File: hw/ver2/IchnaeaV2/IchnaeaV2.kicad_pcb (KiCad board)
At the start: 4 copper layers, 100 x 100 mm, 398 parts, among them J1 Screw_Terminal_01x09, J2 Screw_Terminal_01x09, J3 Screw_Terminal_01x09, J5 FanConnector, J6 Debug, J7 BMS_Serial, P1 USB_C_Plug_USB2.0, Q1 BSS138, Q10 MCAC80N10Y, Q11 MCAC80N10Y, Q12 MCAC80N10Y, Q13 MCAC80N10Y, Q14 MCAC80N10Y, Q15 MCAC80N10Y, Q16 MCAC80N10Y, Q17 MCAC80N10Y, Q18 MCAC80N10Y, Q19 MCAC80N10Y, Q2 MCAC80N10Y, Q20 MCAC80N10Y, Q21 MCAC80N10Y, Q22 MCAC80N10Y, Q23 MCAC80N10Y, Q24 MCAC80N10Y, Q25 MCAC80N10Y, Q26 BSS138, Q27 BSS84, Q28 BSS138, Q29 BSS138, Q3 MCAC80N10Y, Q30 BSS138, Q4 MCAC80N10Y, Q5 MCAC80N10Y, Q6 MCAC80N10Y, Q7 MCAC80N10Y, Q8 MCAC80N10Y, Q9 MCAC80N10Y, SW1 Boot, SW2 Reset, U1 LTC7871, U10 W25Q32JVZP, U11 RP2040, U12 LM1117MP-5.0, U13 LM1117MP-3.3, U14 W25Q32JVZP, U2 HIP2210, U3 HIP2210, U4 HIP2210, U5 HIP2210, U6 HIP2210, U7 HIP2210, U8 AP66200FVBW-13, U9 74HC4051PW, Y1 12MHz

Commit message: Sync work
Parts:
- added D2: ESD9B5.0ST5G, Diode_SMD:D_SOD-923, F.Cu at (87.8, 105.1)
- added D21: ESD9B5.0ST5G, Diode_SMD:D_SOD-923, F.Cu at (87.8, 109.0)
- added D22: SMAJ90A, Diode_SMD:D_SMA, F.Cu at (123.2, 58.8)
- added D23: SMAJ60A, Diode_SMD:D_SMA, F.Cu at (166.8, 58.8)
- added D24: ESD9B5.0ST5G, Diode_SMD:D_SOD-923, F.Cu at (78.1, 140.5)
- added D3: ESD9B5.0ST5G, Diode_SMD:D_SOD-923, F.Cu at (87.8, 107.1)
- added GD1: 90V-2kA, Fuse:Fuse_1812_4532Metric_Pad1.30x3.40mm_HandSolder, F.Cu at (119.3, 58.8)
- added GD2: 90V-2kA, Fuse:Fuse_1812_4532Metric_Pad1.30x3.40mm_HandSolder, F.Cu at (170.5, 58.8)
- added Q31: BSS138, Package_TO_SOT_SMD:SOT-23, F.Cu at (84.0, 106.5)
- added Q32: BSS138, Package_TO_SOT_SMD:SOT-23, F.Cu at (84.0, 111.2)
- added Q33: BSS138, Package_TO_SOT_SMD:SOT-23, F.Cu at (84.0, 115.8)
- added Q34: BSS138, Package_TO_SOT_SMD:SOT-23, F.Cu at (84.0, 120.4)
- added R124: 100, Resistor_SMD:R_0603_1608Metric, F.Cu at (92.1, 110.7)
- added R125: 10k, Resistor_SMD:R_0603_1608Metric, F.Cu at (92.1, 113.2)
- added R126: 100, Resistor_SMD:R_0603_1608Metric, F.Cu at (92.1, 115.7)
- added R127: 10k, Resistor_SMD:R_0603_1608Metric, F.Cu at (92.1, 118.2)
- added R128: 100, Resistor_SMD:R_0603_1608Metric, F.Cu at (92.1, 120.7)
- added R129: 10k, Resistor_SMD:R_0603_1608Metric, F.Cu at (92.1, 123.3)
- added R53: 100k, Resistor_SMD:R_1206_3216Metric, F.Cu at (126.2, 58.8)
- added R55: 100k, Resistor_SMD:R_1206_3216Metric, F.Cu at (163.9, 58.8)
- added TP72: TestPoint, TestPoint:TestPoint_Pad_D1.0mm, F.Cu at (120.0, 148.8)
- added TP73: TestPoint, TestPoint:TestPoint_Pad_D1.0mm, F.Cu at (113.5, 150.5)
- added TP74: TestPoint, TestPoint:TestPoint_Pad_D1.0mm, F.Cu at (115.2, 150.5)
- R106: value 6.2k-0.25w -> 10k; footprint Resistor_SMD:R_1206_3216Metric_Pad1.30x1.75mm_HandSolder -> Resistor_SMD:R_0603_1608Metric
- R31, R35, R78, R81, R93: footprint Resistor_SMD:R_0603_1608Metric -> Resistor_SMD:R_0805_2012Metric
- R33, R39: footprint Resistor_SMD:R_0603_1608Metric_Pad0.98x0.95mm_HandSolder -> Resistor_SMD:R_0805_2012Metric
- R94: value 6.2k-0.25w -> 100; footprint Resistor_SMD:R_1206_3216Metric_Pad1.30x1.75mm_HandSolder -> Resistor_SMD:R_0603_1608Metric
- moved R97 152.1 mm to (182.6, 151.7)
- moved R96 145.4 mm to (174.3, 149.6)
- moved D14 136.7 mm to (185.4, 149.4)
- moved D15 136.7 mm to (185.4, 151.4)
- moved R123 130.5 mm to (182.4, 149.4), turned to 180 degrees
- moved R85 113.1 mm to (143.6, 128.9)
- moved R84 111.3 mm to (123.7, 152.8), turned to 90 degrees
- moved C23 111.0 mm to (105.1, 152.5), turned to -90 degrees
- moved R94 103.1 mm to (92.1, 105.7), turned to 0 degrees
- moved R106 100.7 mm to (92.1, 108.2), turned to 0 degrees
- moved R89 88.8 mm to (103.6, 152.5), turned to -90 degrees
- moved D16 67.1 mm to (115.2, 152.5), turned to 90 degrees
- moved D17 65.1 mm to (113.5, 152.5), turned to 90 degrees
- moved C87 52.1 mm to (128.7, 139.0), turned to 90 degrees
- moved C84 48.6 mm to (123.2, 128.6), turned to 90 degrees
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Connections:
- net /ControlStage/RUN renamed RUN
- net /ControlStage/SWCLK renamed SWCLK
- net /ControlStage/SWDATA renamed SWDATA
- net /ControlStage/UART0_RX renamed UART0_RX
- net /ControlStage/UART0_TX renamed UART0_TX
- net /ControlStage/UART1_RX renamed UART1_RX
- net /ControlStage/UART1_TX renamed UART1_TX
- D14 pad 2: /ControlStage/FAN_CTL -> FAN_CTL
- D15 pad 2: /ControlStage/FAN_SENSE -> FAN_SENSE
- D19 pad 1: /ControlStage/USB_D- -> Net-(D19-A1)
- D20 pad 1: /ControlStage/USB_D+ -> Net-(D20-A1)
- D5 pad 1: /ControlStage/LED_STATUS_0 -> Net-(D5-K)
- D6 pad 1: /ControlStage/LED_STATUS_1 -> Net-(D6-K)
- D7 pad 1: /ControlStage/LED_STATUS_2 -> Net-(D7-K)
- D8 pad 1: /ControlStage/LED_STATUS_3 -> Net-(D8-K)
- P1 pad A6: /ControlStage/USB_D+ -> Net-(D20-A1)
- P1 pad A7: /ControlStage/USB_D- -> Net-(D19-A1)
- P1 pad B6: /ControlStage/USB_D+ -> Net-(D20-A1)
- P1 pad B7: /ControlStage/USB_D- -> Net-(D19-A1)
- R106 pad 2: VHIGH -> Net-(Q34-G)
- R123 pad 1: /ControlStage/FAN_SENSE -> FAN_SENSE
- R94 pad 1: GND -> Net-(Q34-G)
- R94 pad 2: VLOW -> LED_STATUS_3
- R96 pad 1: /ControlStage/FAN_SENSE -> FAN_SENSE
- R97 pad 2: /ControlStage/FAN_CTL -> FAN_CTL
- R98 pad 1: Net-(U11-USB_DP) -> USB_D-
- R98 pad 2: /ControlStage/USB_D+ -> Net-(D19-A1)
- R99 pad 1: Net-(U11-USB_DM) -> USB_D+
- R99 pad 2: /ControlStage/USB_D- -> Net-(D20-A1)
- U11 pad 11: unconnected-(U11-GPIO8-Pad11) -> LTC_CCM
- U11 pad 12: unconnected-(U11-GPIO9-Pad12) -> LTC_DCM
- U11 pad 13: unconnected-(U11-GPIO10-Pad13) -> LTC_SYNC
- U11 pad 14: unconnected-(U11-GPIO11-Pad14) -> /ControlStage/CTL_LTC_PWM_EN
- U11 pad 29: unconnected-(U11-GPIO18-Pad29) -> LED_STATUS_0
- U11 pad 30: unconnected-(U11-GPIO19-Pad30) -> LED_STATUS_1
- U11 pad 34: /ControlStage/FAN_CTL -> LED_STATUS_2
- U11 pad 35: /ControlStage/FAN_SENSE -> LED_STATUS_3
- U11 pad 36: unconnected-(U11-GPIO24-Pad36) -> FAN_CTL
- U11 pad 37: unconnected-(U11-GPIO25-Pad37) -> FAN_SENSE
- U11 pad 46: Net-(U11-USB_DM) -> USB_D-
- U11 pad 47: Net-(U11-USB_DP) -> USB_D+
- U11 pad 6: unconnected-(U11-GPIO4-Pad6) -> ADC_SEL_2
- U11 pad 7: unconnected-(U11-GPIO5-Pad7) -> ADC_SEL_1
- U11 pad 8: unconnected-(U11-GPIO6-Pad8) -> ADC_SEL_0
- U11 pad 9: unconnected-(U11-GPIO7-Pad9) -> LTC_RUN
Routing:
- net GND: track 183.5 -> 265.7 mm, vias 204 -> 223
- net (no net): track 0.00 -> 64.8 mm
- net VHIGH: track 0.00 -> 42.2 mm
- net +3.3V: track 0.00 -> 22.9 mm, vias 0 -> 12
- net /ControlStage/QSPI_SS: track 0.00 -> 22.2 mm, vias 0 -> 2
- net +5V: track 0.00 -> 18.6 mm, vias 0 -> 9
- net Net-(U10-DO(IO1)): track 0.00 -> 15.9 mm
- net Net-(U10-IO2): track 0.00 -> 14.0 mm
- net RUN: track 0.00 -> 12.6 mm
- net Net-(D4-A): track 0.00 -> 12.1 mm
- net Net-(D16-A2): track 0.00 -> 12.1 mm
- net Net-(U12-VI): track 0.00 -> 11.8 mm
- net Net-(P1-CC2): track 0.00 -> 10.9 mm, vias 0 -> 1
- net Net-(P1-CC1): track 0.00 -> 10.1 mm, vias 0 -> 1
- net +1V1: track 0.00 -> 8.57 mm, vias 0 -> 5
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- added copper zone on F.Cu, net +1V1
- added copper zone on F.Cu, net +3.3V
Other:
- board text added: "0"
- board text added: "1"
- board text added: "2"
- board text added: "3"
- board text added: "BOOT"
- board text added: "RESET"

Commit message: Sync to main pc
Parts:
- removed C92: 100nF, Capacitor_SMD:C_0603_1608Metric
- added TP75: TestPoint, TestPoint:TestPoint_Pad_D1.0mm, F.Cu at (132.4, 125.1)
- added TP76: TestPoint, TestPoint:TestPoint_Pad_D1.0mm, F.Cu at (132.4, 120.0)
- moved C104 85.2 mm to (148.9, 132.9)
- moved TP67 77.2 mm to (153.8, 133.6)
- moved TP68 77.2 mm to (153.8, 136.6)
- moved TP69 77.2 mm to (153.8, 139.7)
- moved TP70 77.2 mm to (153.8, 142.7)
- moved R120 73.2 mm to (148.9, 131.3)
- moved C100 65.9 mm to (155.7, 147.1)
- moved C102 65.9 mm to (155.7, 152.1)
- moved R108 65.9 mm to (159.8, 147.1)
- moved R109 65.9 mm to (159.8, 149.6)
- moved R110 65.9 mm to (159.8, 152.1)
- moved R116 65.9 mm to (157.8, 144.5)
- moved C88 55.4 mm to (123.2, 127.4), turned to 90 degrees
- moved C89 49.4 mm to (118.1, 133.2), turned to 180 degrees
- moved C91 49.2 mm to (129.5, 133.2)
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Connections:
- JP3 pad 3: /ControlStage/SPI1_TX -> /ControlStage/SPI0_TX
- JP4 pad 1: /ControlStage/SPI1_TX -> /ControlStage/SPI0_TX
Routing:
- net GND: track 265.7 -> 298.0 mm, vias 223 -> 233
- net SWDATA: track 0.00 -> 31.3 mm
- net RUN: track 12.6 -> 43.7 mm
- net SWCLK: track 0.00 -> 29.7 mm
- net Net-(U11-XIN): track 0.00 -> 20.0 mm
- net Net-(U11-XOUT): track 0.00 -> 18.8 mm
- net UART0_TX: track 0.00 -> 18.5 mm
- net UART1_TX: track 0.00 -> 17.1 mm
- net UART0_RX: track 0.00 -> 16.1 mm
- net UART1_RX: track 0.00 -> 15.8 mm
- net +1V1: track 8.57 -> 18.0 mm, vias 5 -> 6
- net Net-(J7-Pin_2): track 0.00 -> 9.14 mm
- net Net-(J6-Pin_2): track 0.00 -> 8.72 mm
- net +3.3V: track 22.9 -> 28.3 mm, vias 12 -> 13
- net Net-(J7-Pin_1): track 0.00 -> 4.10 mm
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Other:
- board text added: "G"
- board text added: "R"
- board text added: "T"

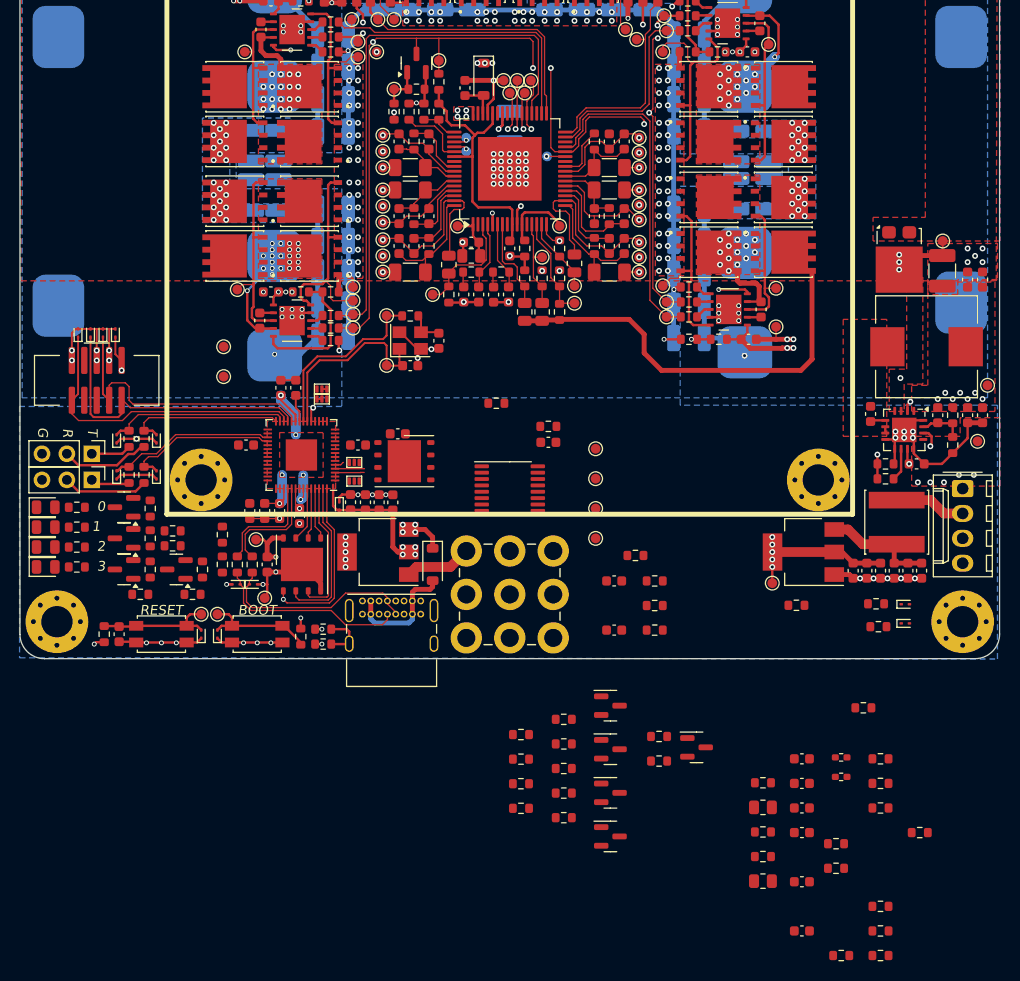
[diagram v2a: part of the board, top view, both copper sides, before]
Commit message: Finish the initial rough route/placement
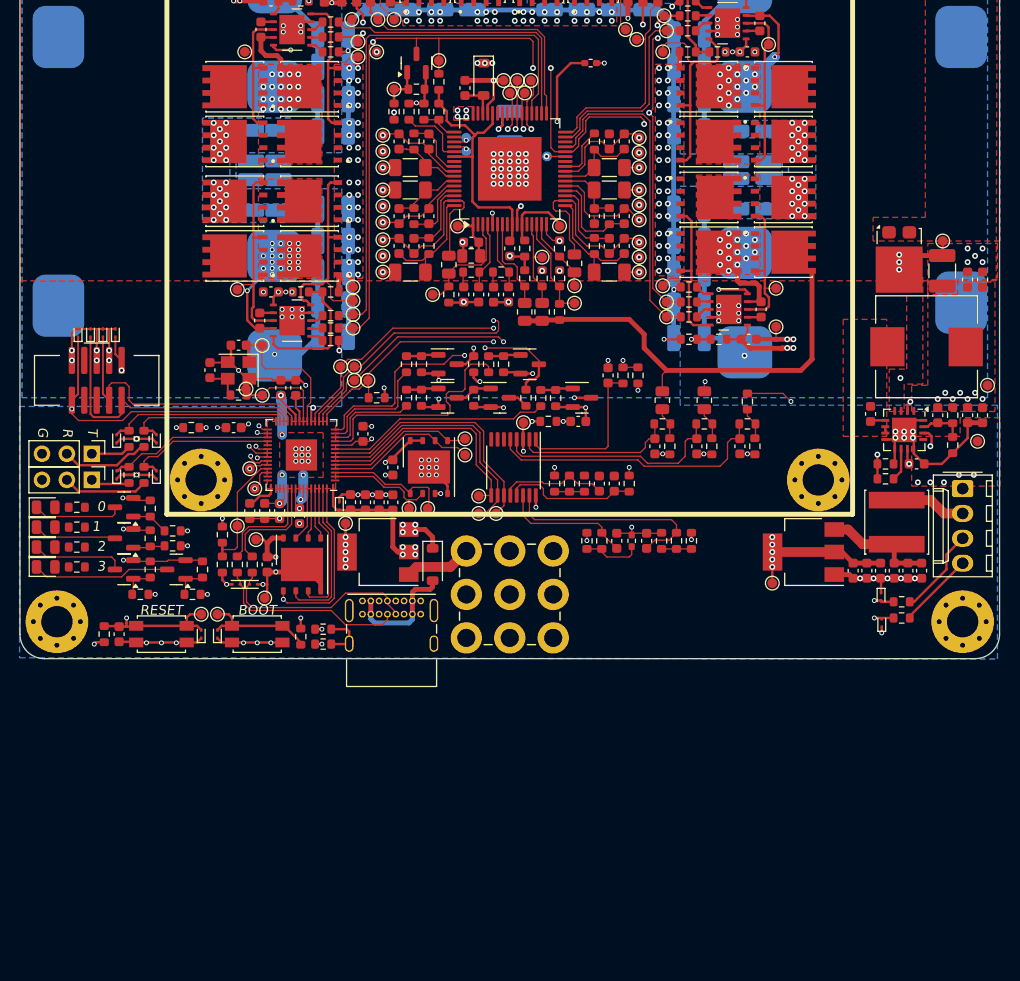
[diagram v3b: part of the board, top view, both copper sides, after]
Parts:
- removed JP1, JP2, JP3, JP4: SolderJumper_3_Bridged12, Jumpers:JumperSolderJumper-3_P0.5mm_Bridged12_0603
- added TP77: TestPoint, TestPoint:TestPoint_Pad_D1.0mm, F.Cu at (136.6, 139.7)
- added TP78: TestPoint, TestPoint:TestPoint_Pad_D1.0mm, F.Cu at (140.4, 134.2)
- added TP79: TestPoint, TestPoint:TestPoint_Pad_D1.0mm, F.Cu at (140.4, 132.6)
- added TP80: TestPoint, TestPoint:TestPoint_Pad_D1.0mm, F.Cu at (134.7, 139.7)
- added TP81: TestPoint, TestPoint:TestPoint_Pad_D1.0mm, F.Cu at (130.5, 126.6)
- added TP82: TestPoint, TestPoint:TestPoint_Pad_D1.0mm, F.Cu at (129.1, 126.6)
- added TP83: TestPoint, TestPoint:TestPoint_Pad_D1.0mm, F.Cu at (129.1, 125.2)
- added TP84: TestPoint, TestPoint:TestPoint_Pad_D1.0mm, F.Cu at (127.7, 125.2)
- added TP85: TestPoint, TestPoint:TestPoint_Pad_D1.0mm, F.Cu at (118.1, 127.5)
- added TP86: TestPoint, TestPoint:TestPoint_Pad_D1.0mm, F.Cu at (119.0, 137.6)
- added TP87: TestPoint, TestPoint:TestPoint_Pad_D1.0mm, F.Cu at (117.2, 141.4)
- added TP88: TestPoint, TestPoint:TestPoint_Pad_D1.0mm, F.Cu at (118.5, 135.6)
- TP64: moved to B.Cu
- moved TH1 75.3 mm to (153.3, 94.2)
- moved R96 64.4 mm to (112.5, 131.4)
- moved Q29 51.0 mm to (138.7, 124.9)
- moved R81 50.2 mm to (160.6, 128.6), turned to 90 degrees
- moved C103 49.9 mm to (168.5, 133.3), turned to -90 degrees
- moved R87 48.9 mm to (154.4, 143.0), turned to 90 degrees
- moved R113 47.2 mm to (162.0, 143.0), turned to 90 degrees
- moved R88 47.1 mm to (156.6, 126.1), turned to -90 degrees
- moved R45 46.7 mm to (144.4, 124.9), turned to 90 degrees
- moved C97 46.1 mm to (155.0, 126.1), turned to 90 degrees
- moved R114 46.0 mm to (169.3, 128.7), turned to -90 degrees
- moved R112 45.7 mm to (160.5, 143.0), turned to -90 degrees
- moved R51 45.6 mm to (141.3, 124.9), turned to -90 degrees
- moved R117 45.3 mm to (169.3, 131.0), turned to 180 degrees
- moved R107 45.1 mm to (160.6, 131.0), turned to 180 degrees
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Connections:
- R81 pad 2: HT -> VHIGH
- R85 pad 1: /ControlStage/CTL_IN_SDI -> /ControlStage/SPI1_RX
- TP2 pad 1: /ControlStage/CTL_OUT_SDO -> /ControlStage/SPI1_TX
- TP3 pad 1: /ControlStage/CTL_IN_SDI -> /ControlStage/SPI1_RX
- U1 pad 38: /ControlStage/CTL_IN_SDI -> /ControlStage/SPI1_RX
- U1 pad 39: /ControlStage/CTL_OUT_SDO -> /ControlStage/SPI1_TX
- U11 pad 38: ADC_SELECTABLE -> ADC_IMON_FLTR
- U11 pad 40: ADC_IMON_FLTR -> ADC_SELECTABLE
- U14 pad 2: /ControlStage/NOR_DO -> /ControlStage/SPI0_RX
- U14 pad 5: /ControlStage/NOR_DI -> /ControlStage/SPI0_TX
- U9 pad 1: 3V3_MON -> TEMP_SENSE_0
- U9 pad 12: 5V0_MON -> 3V3_MON
- U9 pad 13: HV_DC_SENSE -> 1V1_MON
- U9 pad 14: LV_DC_SENSE -> TEMP_SENSE_1
- U9 pad 15: 12V_MON -> 5V0_MON
- U9 pad 2: TEMP_SENSE_0 -> HV_DC_SENSE
- U9 pad 4: TEMP_SENSE_1 -> LV_DC_SENSE
- U9 pad 5: 1V1_MON -> 12V_MON
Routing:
- net FAN_SENSE: track 0.00 -> 101.1 mm, vias 0 -> 3
- net FAN_CTL: track 0.00 -> 86.0 mm, vias 0 -> 2
- net (no net): track 64.8 -> 0.00 mm
- net GND: track 298.0 -> 352.1 mm, vias 233 -> 269
- net /ControlStage/SPI1_TX: track 0.00 -> 52.6 mm, vias 0 -> 2
- net /ControlStage/SPI1_RX: track 0.00 -> 51.3 mm, vias 0 -> 2
- net Net-(R77-Pad1): track 0.00 -> 44.1 mm, vias 0 -> 2
- net ADC_IMON_FLTR: track 0.00 -> 38.1 mm, vias 0 -> 2
- net ADC_SELECTABLE: track 0.00 -> 35.6 mm, vias 0 -> 2
- net +1V1: track 18.0 -> 52.9 mm, vias 6 -> 7
- net LED_STATUS_2: track 0.00 -> 34.7 mm, vias 0 -> 2
- net /ControlStage/CTL_OUT_SDO: track 33.4 -> 0.00 mm, vias 1 -> 0
- net +3.3V: track 28.3 -> 60.9 mm, vias 13 -> 21
- net /ControlStage/CTL_IN_SDI: track 31.8 -> 0.00 mm, vias 1 -> 0
- net LED_STATUS_3: track 0.00 -> 31.0 mm, vias 0 -> 2
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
